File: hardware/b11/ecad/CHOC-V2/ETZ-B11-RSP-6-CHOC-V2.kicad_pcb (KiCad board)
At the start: 2 copper layers, 163.9 x 90.2 mm, 339 parts

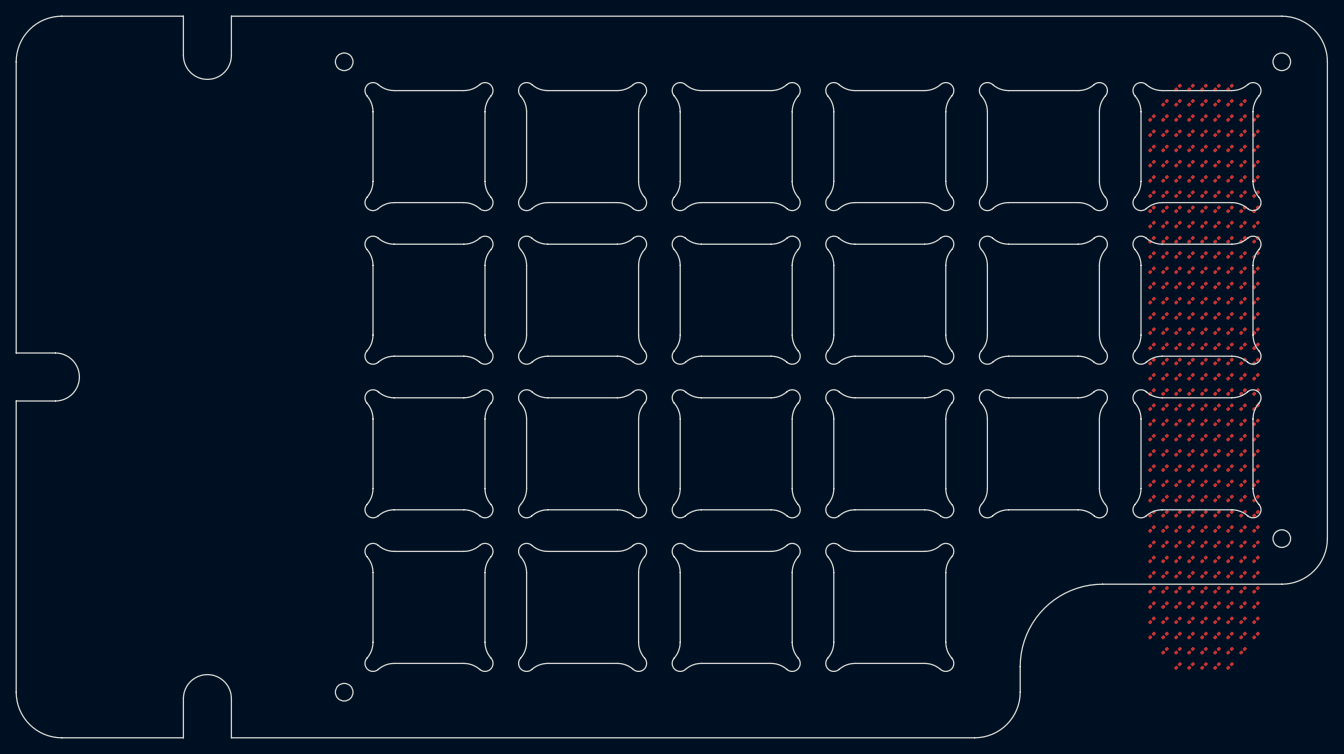
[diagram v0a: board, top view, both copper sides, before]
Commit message: Adjust B11 display LED layout [skip ci]
Signed-off-by: Nikola Secerovski <secersh@gmail.com>
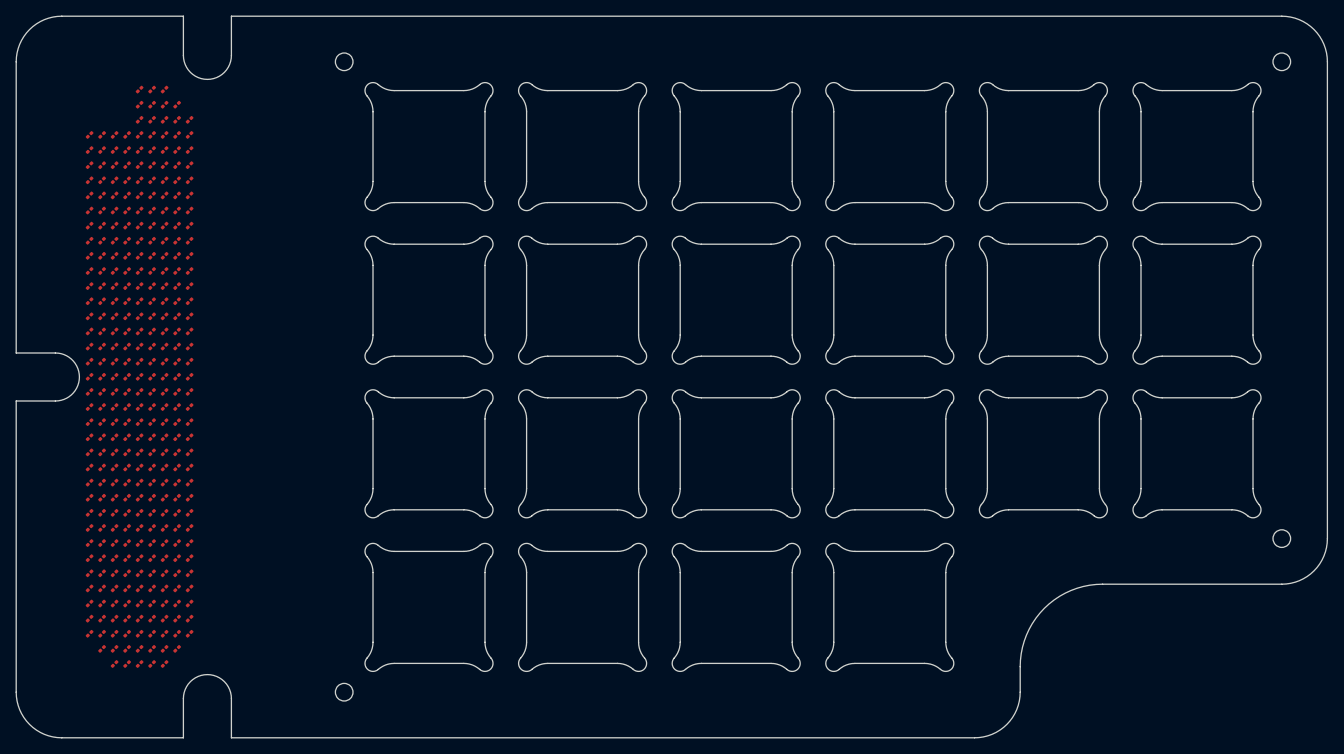
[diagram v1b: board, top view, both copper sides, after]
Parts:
- removed D331, D332, D333, D334, D335, D336, D337, D338, D339: 0201_LED, 0201_LED
- moved D327 141.2 mm to (80.4, 140.2), turned to -135 degrees
- moved D326 141.1 mm to (78.8, 140.2), turned to -135 degrees
- moved D5 134.8 mm to (83.5, 70.3), turned to -135 degrees
- moved D4 134.7 mm to (82.0, 70.3), turned to -135 degrees
- moved D21 133.3 mm to (88.2, 74.0), turned to -135 degrees
- moved D30 133.3 mm to (88.2, 75.9), turned to -135 degrees
- moved D39 133.3 mm to (88.2, 77.8), turned to -135 degrees
- moved D48 133.3 mm to (88.2, 79.7), turned to -135 degrees
- moved D57 133.3 mm to (88.2, 81.6), turned to -135 degrees
- moved D66 133.3 mm to (88.2, 83.5), turned to -135 degrees
- moved D75 133.3 mm to (88.2, 85.4), turned to -135 degrees
- moved D84 133.3 mm to (88.2, 87.3), turned to -135 degrees
- moved D93 133.3 mm to (88.2, 89.2), turned to -135 degrees
- moved D102 133.3 mm to (88.2, 91.0), turned to -135 degrees
- moved D111 133.3 mm to (88.2, 92.9), turned to -135 degrees
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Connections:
- D1 pad 2: LED_SW3 -> LED_SW5
- D10 pad 1: LED_CS2 -> LED_CS3
- D10 pad 2: LED_SW6 -> LED_SW7
- D100 pad 1: LED_CS12 -> LED_CS13
- D101 pad 1: LED_CS12 -> LED_CS13
- D102 pad 1: LED_CS12 -> LED_CS13
- D103 pad 1: LED_CS13 -> LED_CS14
- D104 pad 1: LED_CS13 -> LED_CS14
- D105 pad 1: LED_CS13 -> LED_CS14
- D106 pad 1: LED_CS13 -> LED_CS14
- D107 pad 1: LED_CS13 -> LED_CS14
- D108 pad 1: LED_CS13 -> LED_CS14
- D109 pad 1: LED_CS13 -> LED_CS14
- D11 pad 1: LED_CS2 -> LED_CS3
- D11 pad 2: LED_SW7 -> LED_SW8
- D110 pad 1: LED_CS13 -> LED_CS14
- D111 pad 1: LED_CS13 -> LED_CS14
- D112 pad 1: LED_CS14 -> LED_CS15
- D113 pad 1: LED_CS14 -> LED_CS15
- D114 pad 1: LED_CS14 -> LED_CS15
- D115 pad 1: LED_CS14 -> LED_CS15
- D116 pad 1: LED_CS14 -> LED_CS15
- D117 pad 1: LED_CS14 -> LED_CS15
- D118 pad 1: LED_CS14 -> LED_CS15
- D119 pad 1: LED_CS14 -> LED_CS15
- D12 pad 1: LED_CS2 -> LED_CS3
- D12 pad 2: LED_SW8 -> LED_SW9
- D120 pad 1: LED_CS14 -> LED_CS15
- D121 pad 1: LED_CS15 -> LED_CS16
- D122 pad 1: LED_CS15 -> LED_CS16
- D123 pad 1: LED_CS15 -> LED_CS16
- D124 pad 1: LED_CS15 -> LED_CS16
- D125 pad 1: LED_CS15 -> LED_CS16
- D126 pad 1: LED_CS15 -> LED_CS16
- D127 pad 1: LED_CS15 -> LED_CS16
- D128 pad 1: LED_CS15 -> LED_CS16
- D129 pad 1: LED_CS15 -> LED_CS16
- D13 pad 1: LED_CS3 -> LED_CS4
- D130 pad 1: LED_CS16 -> LED_CS17
- D131 pad 1: LED_CS16 -> LED_CS17
- D132 pad 1: LED_CS16 -> LED_CS17
- D133 pad 1: LED_CS16 -> LED_CS17
- D134 pad 1: LED_CS16 -> LED_CS17
- D135 pad 1: LED_CS16 -> LED_CS17
- D136 pad 1: LED_CS16 -> LED_CS17
- D137 pad 1: LED_CS16 -> LED_CS17
- D138 pad 1: LED_CS16 -> LED_CS17
- D139 pad 1: LED_CS17 -> LED_CS18
- D14 pad 1: LED_CS3 -> LED_CS4
- D140 pad 1: LED_CS17 -> LED_CS18
- D141 pad 1: LED_CS17 -> LED_CS18
- D142 pad 1: LED_CS17 -> LED_CS18
- D143 pad 1: LED_CS17 -> LED_CS18
- D144 pad 1: LED_CS17 -> LED_CS18
- D145 pad 1: LED_CS17 -> LED_CS18
- D146 pad 1: LED_CS17 -> LED_CS18
- D147 pad 1: LED_CS17 -> LED_CS18
- D148 pad 1: LED_CS18 -> LED_CS19
- D149 pad 1: LED_CS18 -> LED_CS19
- D15 pad 1: LED_CS3 -> LED_CS4
- D150 pad 1: LED_CS18 -> LED_CS19
- D151 pad 1: LED_CS18 -> LED_CS19
- D152 pad 1: LED_CS18 -> LED_CS19
- D153 pad 1: LED_CS18 -> LED_CS19
- D154 pad 1: LED_CS18 -> LED_CS19
- D155 pad 1: LED_CS18 -> LED_CS19
- D156 pad 1: LED_CS18 -> LED_CS19
- D157 pad 1: LED_CS19 -> LED_CS20
- D158 pad 1: LED_CS19 -> LED_CS20
- D159 pad 1: LED_CS19 -> LED_CS20
- D16 pad 1: LED_CS3 -> LED_CS4
- D160 pad 1: LED_CS19 -> LED_CS20
- D161 pad 1: LED_CS19 -> LED_CS20
- D162 pad 1: LED_CS19 -> LED_CS20
- D163 pad 1: LED_CS19 -> LED_CS20
- D164 pad 1: LED_CS19 -> LED_CS20
- D165 pad 1: LED_CS19 -> LED_CS20
- D166 pad 1: LED_CS20 -> LED_CS21
- D167 pad 1: LED_CS20 -> LED_CS21
- D168 pad 1: LED_CS20 -> LED_CS21
- D169 pad 1: LED_CS20 -> LED_CS21
- D17 pad 1: LED_CS3 -> LED_CS4
- D170 pad 1: LED_CS20 -> LED_CS21
- D171 pad 1: LED_CS20 -> LED_CS21
- D172 pad 1: LED_CS20 -> LED_CS21
- D173 pad 1: LED_CS20 -> LED_CS21
- D174 pad 1: LED_CS20 -> LED_CS21
- D175 pad 1: LED_CS21 -> LED_CS22
- D176 pad 1: LED_CS21 -> LED_CS22
- D177 pad 1: LED_CS21 -> LED_CS22
- D178 pad 1: LED_CS21 -> LED_CS22
- D179 pad 1: LED_CS21 -> LED_CS22
- D18 pad 1: LED_CS3 -> LED_CS4
- D180 pad 1: LED_CS21 -> LED_CS22
- D181 pad 1: LED_CS21 -> LED_CS22
- D182 pad 1: LED_CS21 -> LED_CS22
- D183 pad 1: LED_CS21 -> LED_CS22
- D184 pad 1: LED_CS22 -> LED_CS23
- D185 pad 1: LED_CS22 -> LED_CS23
- D186 pad 1: LED_CS22 -> LED_CS23
- D187 pad 1: LED_CS22 -> LED_CS23
- D188 pad 1: LED_CS22 -> LED_CS23
- D189 pad 1: LED_CS22 -> LED_CS23
- D19 pad 1: LED_CS3 -> LED_CS4
- D190 pad 1: LED_CS22 -> LED_CS23
- D191 pad 1: LED_CS22 -> LED_CS23
- D192 pad 1: LED_CS22 -> LED_CS23
- D193 pad 1: LED_CS23 -> LED_CS24
- D194 pad 1: LED_CS23 -> LED_CS24
- D195 pad 1: LED_CS23 -> LED_CS24
- D196 pad 1: LED_CS23 -> LED_CS24
- D197 pad 1: LED_CS23 -> LED_CS24
- D198 pad 1: LED_CS23 -> LED_CS24
- D199 pad 1: LED_CS23 -> LED_CS24
- D2 pad 2: LED_SW4 -> LED_SW6
- D20 pad 1: LED_CS3 -> LED_CS4
- D200 pad 1: LED_CS23 -> LED_CS24
- D201 pad 1: LED_CS23 -> LED_CS24
- D202 pad 1: LED_CS24 -> LED_CS25
- D203 pad 1: LED_CS24 -> LED_CS25
- D204 pad 1: LED_CS24 -> LED_CS25
- D205 pad 1: LED_CS24 -> LED_CS25
- D206 pad 1: LED_CS24 -> LED_CS25
- D207 pad 1: LED_CS24 -> LED_CS25
- D208 pad 1: LED_CS24 -> LED_CS25
- D209 pad 1: LED_CS24 -> LED_CS25
- D21 pad 1: LED_CS3 -> LED_CS4
- D210 pad 1: LED_CS24 -> LED_CS25
- D211 pad 1: LED_CS25 -> LED_CS26
- D212 pad 1: LED_CS25 -> LED_CS26
- D213 pad 1: LED_CS25 -> LED_CS26
- D214 pad 1: LED_CS25 -> LED_CS26
- D215 pad 1: LED_CS25 -> LED_CS26
- D216 pad 1: LED_CS25 -> LED_CS26
- D217 pad 1: LED_CS25 -> LED_CS26
- D218 pad 1: LED_CS25 -> LED_CS26
- D219 pad 1: LED_CS25 -> LED_CS26
- D22 pad 1: LED_CS4 -> LED_CS5
- D220 pad 1: LED_CS26 -> LED_CS27
- D221 pad 1: LED_CS26 -> LED_CS27
- D222 pad 1: LED_CS26 -> LED_CS27
- D223 pad 1: LED_CS26 -> LED_CS27
- D224 pad 1: LED_CS26 -> LED_CS27
- D225 pad 1: LED_CS26 -> LED_CS27
- D226 pad 1: LED_CS26 -> LED_CS27
- D227 pad 1: LED_CS26 -> LED_CS27
- D228 pad 1: LED_CS26 -> LED_CS27
- D229 pad 1: LED_CS27 -> LED_CS28
- D23 pad 1: LED_CS4 -> LED_CS5
- D230 pad 1: LED_CS27 -> LED_CS28
- D231 pad 1: LED_CS27 -> LED_CS28
- D232 pad 1: LED_CS27 -> LED_CS28
- D233 pad 1: LED_CS27 -> LED_CS28
- D234 pad 1: LED_CS27 -> LED_CS28
- D235 pad 1: LED_CS27 -> LED_CS28
- D236 pad 1: LED_CS27 -> LED_CS28
- D237 pad 1: LED_CS27 -> LED_CS28
- D238 pad 1: LED_CS28 -> LED_CS29
- D239 pad 1: LED_CS28 -> LED_CS29
- D24 pad 1: LED_CS4 -> LED_CS5
- D240 pad 1: LED_CS28 -> LED_CS29
- D241 pad 1: LED_CS28 -> LED_CS29
- D242 pad 1: LED_CS28 -> LED_CS29
- D243 pad 1: LED_CS28 -> LED_CS29
- D244 pad 1: LED_CS28 -> LED_CS29
- D245 pad 1: LED_CS28 -> LED_CS29
- D246 pad 1: LED_CS28 -> LED_CS29
- D247 pad 1: LED_CS29 -> LED_CS30
- D248 pad 1: LED_CS29 -> LED_CS30
- D249 pad 1: LED_CS29 -> LED_CS30
- D25 pad 1: LED_CS4 -> LED_CS5
- D250 pad 1: LED_CS29 -> LED_CS30
- D251 pad 1: LED_CS29 -> LED_CS30
- D252 pad 1: LED_CS29 -> LED_CS30
- D253 pad 1: LED_CS29 -> LED_CS30
- D254 pad 1: LED_CS29 -> LED_CS30
- D255 pad 1: LED_CS29 -> LED_CS30
- D256 pad 1: LED_CS30 -> LED_CS31
- D257 pad 1: LED_CS30 -> LED_CS31
- D258 pad 1: LED_CS30 -> LED_CS31
- D259 pad 1: LED_CS30 -> LED_CS31
- D26 pad 1: LED_CS4 -> LED_CS5
- D260 pad 1: LED_CS30 -> LED_CS31
- D261 pad 1: LED_CS30 -> LED_CS31
- D262 pad 1: LED_CS30 -> LED_CS31
- D263 pad 1: LED_CS30 -> LED_CS31
- D264 pad 1: LED_CS30 -> LED_CS31
- D265 pad 1: LED_CS31 -> LED_CS32
- D266 pad 1: LED_CS31 -> LED_CS32
- D267 pad 1: LED_CS31 -> LED_CS32
- D268 pad 1: LED_CS31 -> LED_CS32
- D269 pad 1: LED_CS31 -> LED_CS32
- D27 pad 1: LED_CS4 -> LED_CS5
- D270 pad 1: LED_CS31 -> LED_CS32
- D271 pad 1: LED_CS31 -> LED_CS32
- D272 pad 1: LED_CS31 -> LED_CS32
- D273 pad 1: LED_CS31 -> LED_CS32
- D274 pad 1: LED_CS32 -> LED_CS33
- D275 pad 1: LED_CS32 -> LED_CS33
- D276 pad 1: LED_CS32 -> LED_CS33
- D277 pad 1: LED_CS32 -> LED_CS33
- D278 pad 1: LED_CS32 -> LED_CS33
- D279 pad 1: LED_CS32 -> LED_CS33
- D28 pad 1: LED_CS4 -> LED_CS5
- D280 pad 1: LED_CS32 -> LED_CS33
- D281 pad 1: LED_CS32 -> LED_CS33
- D282 pad 1: LED_CS32 -> LED_CS33
- D283 pad 1: LED_CS33 -> LED_CS34
- D284 pad 1: LED_CS33 -> LED_CS34
- D285 pad 1: LED_CS33 -> LED_CS34
- D286 pad 1: LED_CS33 -> LED_CS34
- D287 pad 1: LED_CS33 -> LED_CS34
- D288 pad 1: LED_CS33 -> LED_CS34
- D289 pad 1: LED_CS33 -> LED_CS34
- D29 pad 1: LED_CS4 -> LED_CS5
- D290 pad 1: LED_CS33 -> LED_CS34
- D291 pad 1: LED_CS33 -> LED_CS34
- D292 pad 1: LED_CS34 -> LED_CS35
- D293 pad 1: LED_CS34 -> LED_CS35
- D294 pad 1: LED_CS34 -> LED_CS35
- D295 pad 1: LED_CS34 -> LED_CS35
- D296 pad 1: LED_CS34 -> LED_CS35
- D297 pad 1: LED_CS34 -> LED_CS35
- D298 pad 1: LED_CS34 -> LED_CS35
- D299 pad 1: LED_CS34 -> LED_CS35
- D3 pad 2: LED_SW5 -> LED_SW7
- D30 pad 1: LED_CS4 -> LED_CS5
- D300 pad 1: LED_CS34 -> LED_CS35
- D301 pad 1: LED_CS35 -> LED_CS36
- D302 pad 1: LED_CS35 -> LED_CS36
- D303 pad 1: LED_CS35 -> LED_CS36
- D304 pad 1: LED_CS35 -> LED_CS36
- D305 pad 1: LED_CS35 -> LED_CS36
- D306 pad 1: LED_CS35 -> LED_CS36
- D307 pad 1: LED_CS35 -> LED_CS36
- D308 pad 1: LED_CS35 -> LED_CS36
- D309 pad 1: LED_CS35 -> LED_CS36
- D31 pad 1: LED_CS5 -> LED_CS6
- D310 pad 1: LED_CS36 -> LED_CS37
- D311 pad 1: LED_CS36 -> LED_CS37
- D312 pad 1: LED_CS36 -> LED_CS37
- D313 pad 1: LED_CS36 -> LED_CS37
- D314 pad 1: LED_CS36 -> LED_CS37
- D315 pad 1: LED_CS36 -> LED_CS37
- D316 pad 1: LED_CS36 -> LED_CS37
- D317 pad 1: LED_CS36 -> LED_CS37
- D318 pad 1: LED_CS36 -> LED_CS37
- D319 pad 1: LED_CS37 -> LED_CS38
- D319 pad 2: LED_SW1 -> LED_SW2
- D32 pad 1: LED_CS5 -> LED_CS6
- D320 pad 1: LED_CS37 -> LED_CS38
- D320 pad 2: LED_SW2 -> LED_SW3
- D321 pad 1: LED_CS37 -> LED_CS38
- D321 pad 2: LED_SW3 -> LED_SW4
- D322 pad 1: LED_CS37 -> LED_CS38
- D322 pad 2: LED_SW4 -> LED_SW5
- D323 pad 1: LED_CS37 -> LED_CS38
- D323 pad 2: LED_SW5 -> LED_SW6
- D324 pad 1: LED_CS37 -> LED_CS38
- D324 pad 2: LED_SW6 -> LED_SW7
- D325 pad 1: LED_CS37 -> LED_CS38
- D325 pad 2: LED_SW7 -> LED_SW8
- D326 pad 1: LED_CS37 -> LED_CS39
- D326 pad 2: LED_SW8 -> LED_SW3
- D327 pad 1: LED_CS37 -> LED_CS39
- D327 pad 2: LED_SW9 -> LED_SW4
- D328 pad 1: LED_CS38 -> LED_CS39
- D328 pad 2: LED_SW2 -> LED_SW5
- D329 pad 1: LED_CS38 -> LED_CS39
- D329 pad 2: LED_SW3 -> LED_SW6
- D33 pad 1: LED_CS5 -> LED_CS6
- D330 pad 1: LED_CS38 -> LED_CS39
- D330 pad 2: LED_SW4 -> LED_SW7
- D34 pad 1: LED_CS5 -> LED_CS6
- D35 pad 1: LED_CS5 -> LED_CS6
- D36 pad 1: LED_CS5 -> LED_CS6
- D37 pad 1: LED_CS5 -> LED_CS6
- D38 pad 1: LED_CS5 -> LED_CS6
- D39 pad 1: LED_CS5 -> LED_CS6
- D4 pad 1: LED_CS1 -> LED_CS2
- D4 pad 2: LED_SW6 -> LED_SW5
- D40 pad 1: LED_CS6 -> LED_CS7
- D41 pad 1: LED_CS6 -> LED_CS7
- D42 pad 1: LED_CS6 -> LED_CS7
- D43 pad 1: LED_CS6 -> LED_CS7
- D44 pad 1: LED_CS6 -> LED_CS7
- D45 pad 1: LED_CS6 -> LED_CS7
- D46 pad 1: LED_CS6 -> LED_CS7
- D47 pad 1: LED_CS6 -> LED_CS7
- D48 pad 1: LED_CS6 -> LED_CS7
- D49 pad 1: LED_CS7 -> LED_CS8
- D5 pad 1: LED_CS1 -> LED_CS2
- D5 pad 2: LED_SW7 -> LED_SW6
- D50 pad 1: LED_CS7 -> LED_CS8
- D51 pad 1: LED_CS7 -> LED_CS8
- D52 pad 1: LED_CS7 -> LED_CS8
- D53 pad 1: LED_CS7 -> LED_CS8
- D54 pad 1: LED_CS7 -> LED_CS8
- D55 pad 1: LED_CS7 -> LED_CS8
- D56 pad 1: LED_CS7 -> LED_CS8
- D57 pad 1: LED_CS7 -> LED_CS8
- D58 pad 1: LED_CS8 -> LED_CS9
- D59 pad 1: LED_CS8 -> LED_CS9
- D6 pad 2: LED_SW2 -> LED_SW7
- D60 pad 1: LED_CS8 -> LED_CS9
- D61 pad 1: LED_CS8 -> LED_CS9
- D62 pad 1: LED_CS8 -> LED_CS9
- D63 pad 1: LED_CS8 -> LED_CS9
- D64 pad 1: LED_CS8 -> LED_CS9
- D65 pad 1: LED_CS8 -> LED_CS9
- D66 pad 1: LED_CS8 -> LED_CS9
- D67 pad 1: LED_CS9 -> LED_CS10
- D68 pad 1: LED_CS9 -> LED_CS10
- D69 pad 1: LED_CS9 -> LED_CS10
- D7 pad 2: LED_SW3 -> LED_SW8
- D70 pad 1: LED_CS9 -> LED_CS10
- D71 pad 1: LED_CS9 -> LED_CS10
- D72 pad 1: LED_CS9 -> LED_CS10
- D73 pad 1: LED_CS9 -> LED_CS10
- D74 pad 1: LED_CS9 -> LED_CS10
- D75 pad 1: LED_CS9 -> LED_CS10
- D76 pad 1: LED_CS10 -> LED_CS11
- D77 pad 1: LED_CS10 -> LED_CS11
- D78 pad 1: LED_CS10 -> LED_CS11
- D79 pad 1: LED_CS10 -> LED_CS11
- D8 pad 1: LED_CS2 -> LED_CS3
- D8 pad 2: LED_SW4 -> LED_SW5
- D80 pad 1: LED_CS10 -> LED_CS11
- D81 pad 1: LED_CS10 -> LED_CS11
- D82 pad 1: LED_CS10 -> LED_CS11
- D83 pad 1: LED_CS10 -> LED_CS11
- D84 pad 1: LED_CS10 -> LED_CS11
- D85 pad 1: LED_CS11 -> LED_CS12
- D86 pad 1: LED_CS11 -> LED_CS12
- D87 pad 1: LED_CS11 -> LED_CS12
- D88 pad 1: LED_CS11 -> LED_CS12
- D89 pad 1: LED_CS11 -> LED_CS12
- D9 pad 1: LED_CS2 -> LED_CS3
- D9 pad 2: LED_SW5 -> LED_SW6
- D90 pad 1: LED_CS11 -> LED_CS12
- D91 pad 1: LED_CS11 -> LED_CS12
- D92 pad 1: LED_CS11 -> LED_CS12
- D93 pad 1: LED_CS11 -> LED_CS12
- D94 pad 1: LED_CS12 -> LED_CS13
- D95 pad 1: LED_CS12 -> LED_CS13
- D96 pad 1: LED_CS12 -> LED_CS13
- D97 pad 1: LED_CS12 -> LED_CS13
- D98 pad 1: LED_CS12 -> LED_CS13
- D99 pad 1: LED_CS12 -> LED_CS13

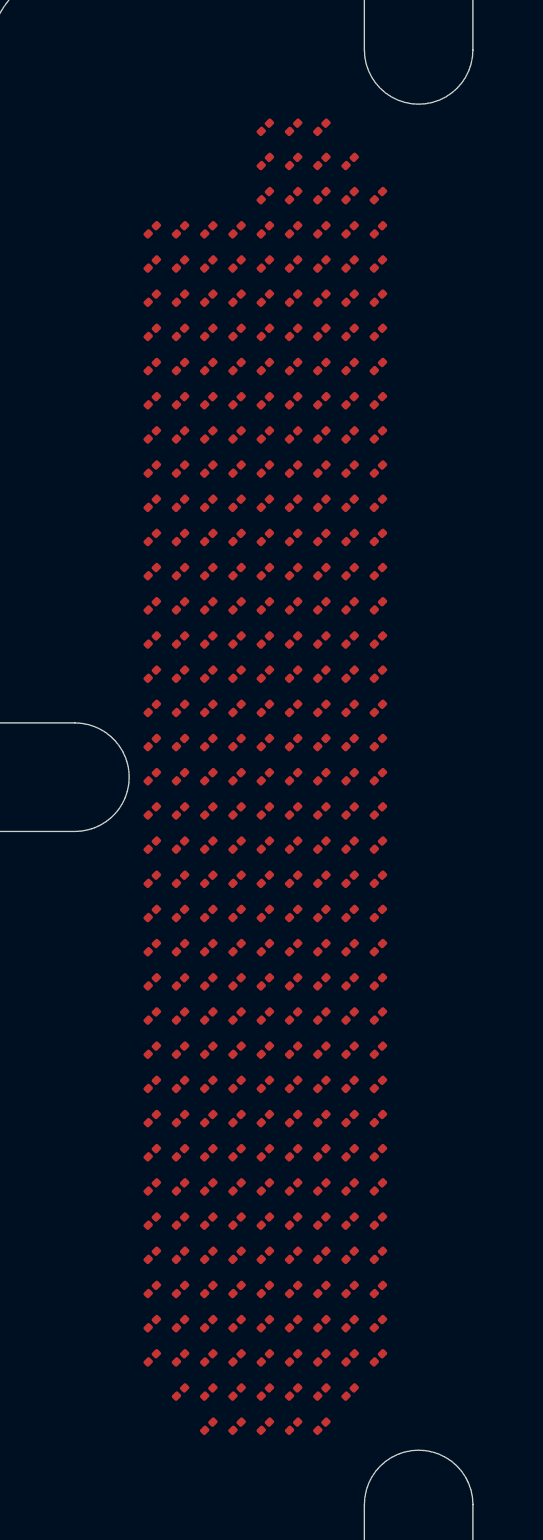
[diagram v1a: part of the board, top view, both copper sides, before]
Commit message: Route B11 display LED matrix [skip ci]
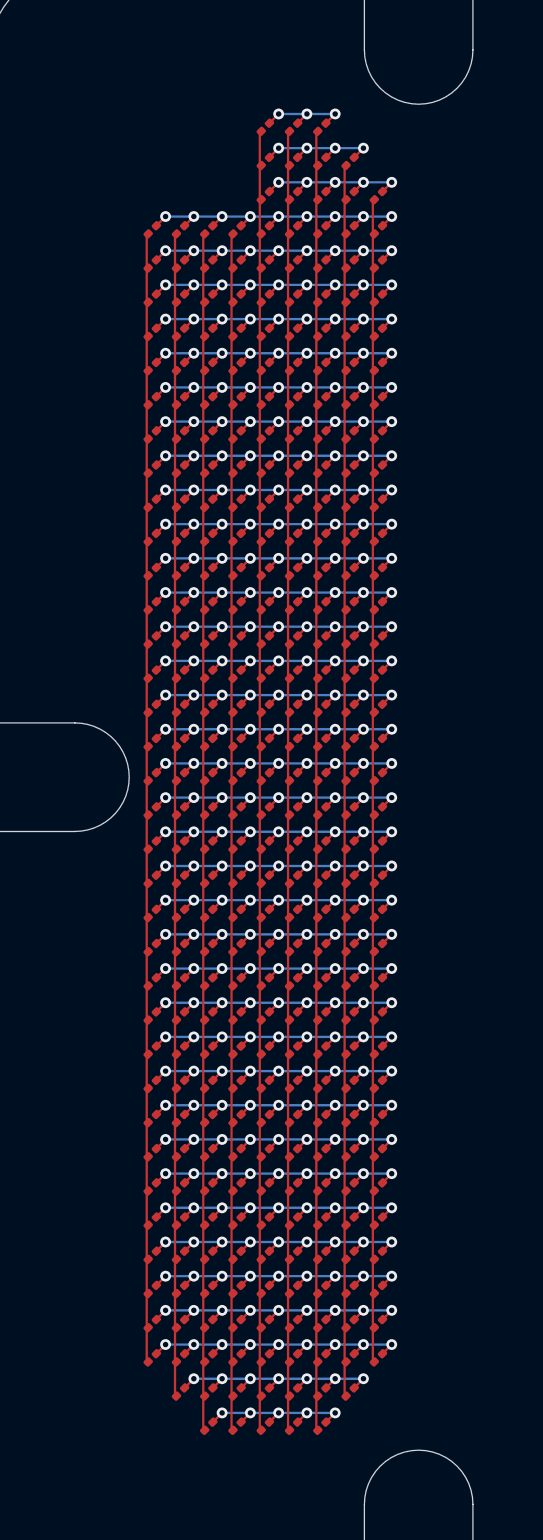
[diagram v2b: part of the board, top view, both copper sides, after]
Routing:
- net LED_SW7: track 0.00 -> 74.9 mm
- net LED_SW6: track 0.00 -> 74.9 mm
- net LED_SW5: track 0.00 -> 74.9 mm
- net LED_SW8: track 0.00 -> 71.0 mm
- net LED_SW4: track 0.00 -> 69.0 mm
- net LED_SW3: track 0.00 -> 69.0 mm
- net LED_SW2: track 0.00 -> 67.0 mm
- net LED_SW9: track 0.00 -> 67.0 mm
- net LED_SW1: track 0.00 -> 65.1 mm
- net LED_CS9: track 0.00 -> 19.0 mm, vias 0 -> 9
- net LED_CS7: track 0.00 -> 19.0 mm, vias 0 -> 9
- net LED_CS5: track 0.00 -> 19.0 mm, vias 0 -> 9
- net LED_CS4: track 0.00 -> 19.0 mm, vias 0 -> 9
- net LED_CS37: track 0.00 -> 19.0 mm, vias 0 -> 9
- net LED_CS36: track 0.00 -> 19.0 mm, vias 0 -> 9
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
